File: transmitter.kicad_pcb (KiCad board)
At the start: 6 copper layers, 200 x 110 mm, 244 parts, among them IC1 W9864G6KH-6, IC2 TPS61165DBVR, IC3 MT25QL128ABA1ESE-0SIT, IC4 USBLC6-2SC6, J1 AFC01-S40FCA-00, J2 AFC07-S10ECC-00, J3 B2B-PH-K-S, J4 B2B-PH-K-S, J5 B3B-PH-K-S, J6 USB4085-GF-A, J7 Conn_01x05, J9 Conn_02x06_Odd_Even, Q1 AO3400A, Q2 AO3400A, Q3 SI2301CDS-T1-GE3, Q4 AO3400A, SW1 Button SPST SMD Tactile Switch, SW2 Button SPST SMD Tactile Switch, SW3 Button SPST SMD Tactile Switch, SW4 Button SPST SMD Tactile Switch, SW5 Button SPST SMD Tactile Switch, SW6 Button SPST SMD Tactile Switch, SW7 SW_SPDT_MSM, SW8 Button SPST SMD Tactile Switch, SW9 RotaryEncoder_Switch, U1 STM32H743ZIT6TR, U2 CAT24C256, U3 MP2667GG-0000-Z, U4 AMS1117-3.3, U5 TPS61252DSG, U6 PCA9554APW, Y1 32.768KHZ, Y2 X322525MOB4SI-25MHz

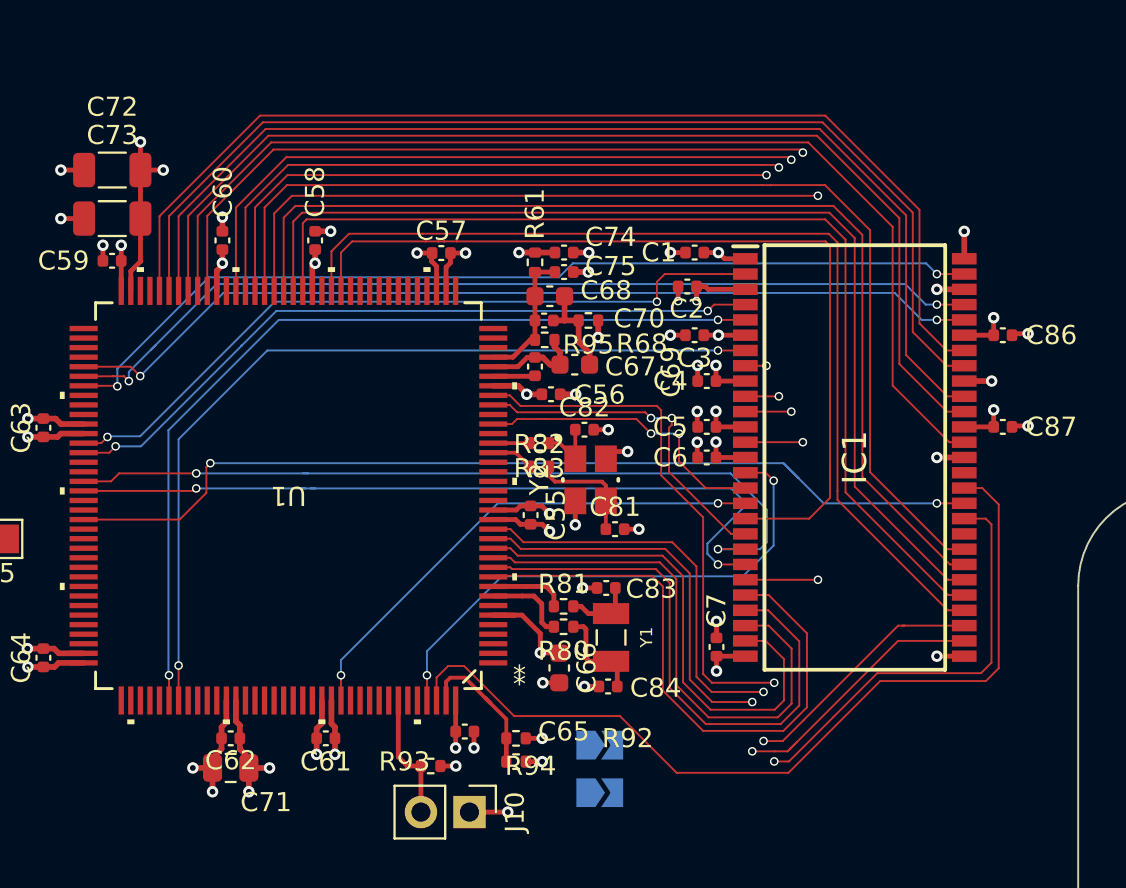
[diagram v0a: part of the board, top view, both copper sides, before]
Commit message: trace length matching sdram, almost done 80%
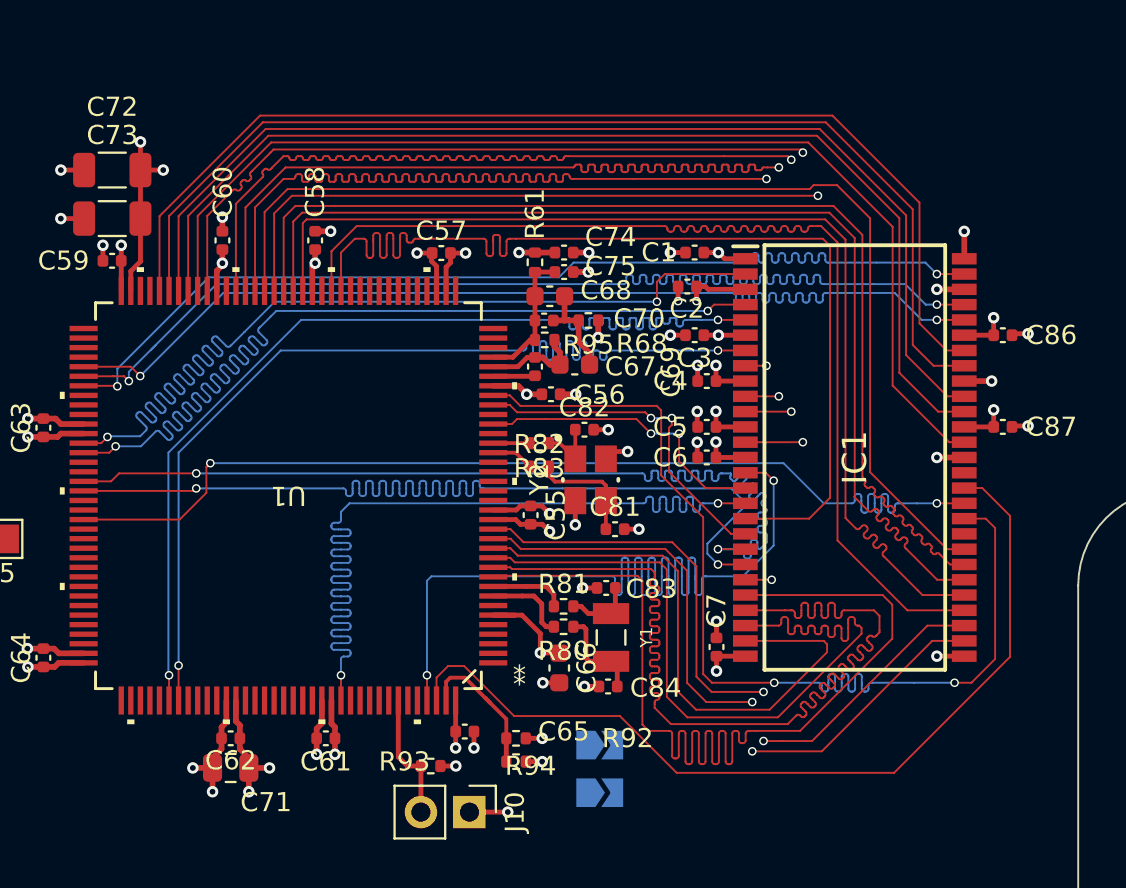
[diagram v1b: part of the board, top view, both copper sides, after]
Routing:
- net /Project Architecture/MCU - IO/FMC_SDNCAS: track 26.7 -> 53.7 mm
- net /Project Architecture/MCU - IO/FMC_A1: track 29.9 -> 56.5 mm
- net /Project Architecture/MCU - IO/FMC_NBL0: track 28.1 -> 53.8 mm
- net /Project Architecture/MCU - IO/FMC_A0: track 31.4 -> 56.9 mm
- net /Project Architecture/MCU - IO/FMC_D1: track 37.9 -> 53.7 mm
- net /Project Architecture/MCU - IO/FMC_D0: track 38.9 -> 53.8 mm
- net /Project Architecture/MCU - IO/FMC_BA1: track 41.1 -> 53.8 mm
- net /Project Architecture/MCU - IO/FMC_A2: track 28.4 -> 40.6 mm
- net /Project Architecture/MCU - IO/FMC_D4: track 42.9 -> 55.0 mm
- net /Project Architecture/MCU - IO/FMC_BA0: track 42.8 -> 53.7 mm
- net /Project Architecture/MCU - IO/FMC_SDNRAS: track 46.0 -> 56.9 mm
- net /Project Architecture/MCU - IO/FMC_D14: track 49.4 -> 60.1 mm
- net /Project Architecture/MCU - IO/FMC_D3: track 45.3 -> 53.8 mm
- net /Project Architecture/MCU - IO/FMC_D5: track 47.0 -> 55.1 mm
- net /Project Architecture/MCU - IO/FMC_D2: track 46.7 -> 53.9 mm
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
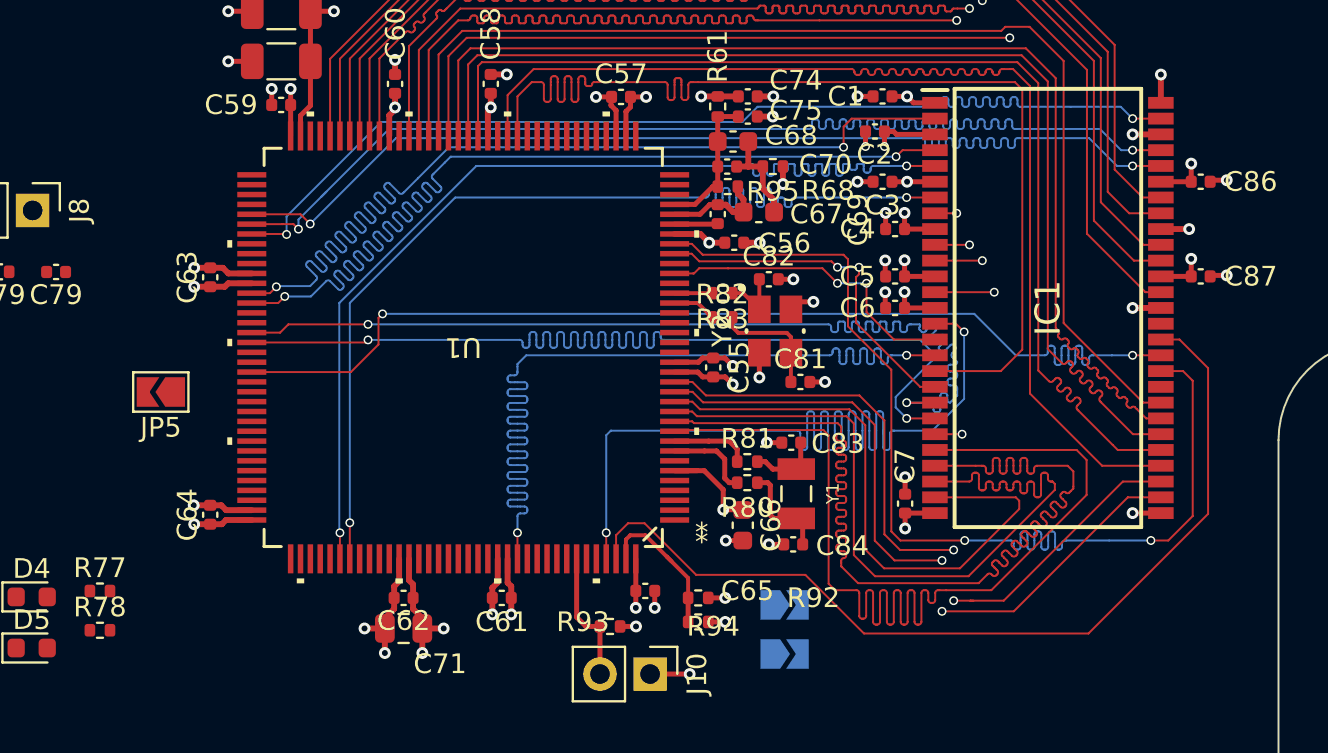
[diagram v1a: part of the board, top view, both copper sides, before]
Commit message: sdram routed and length matching done
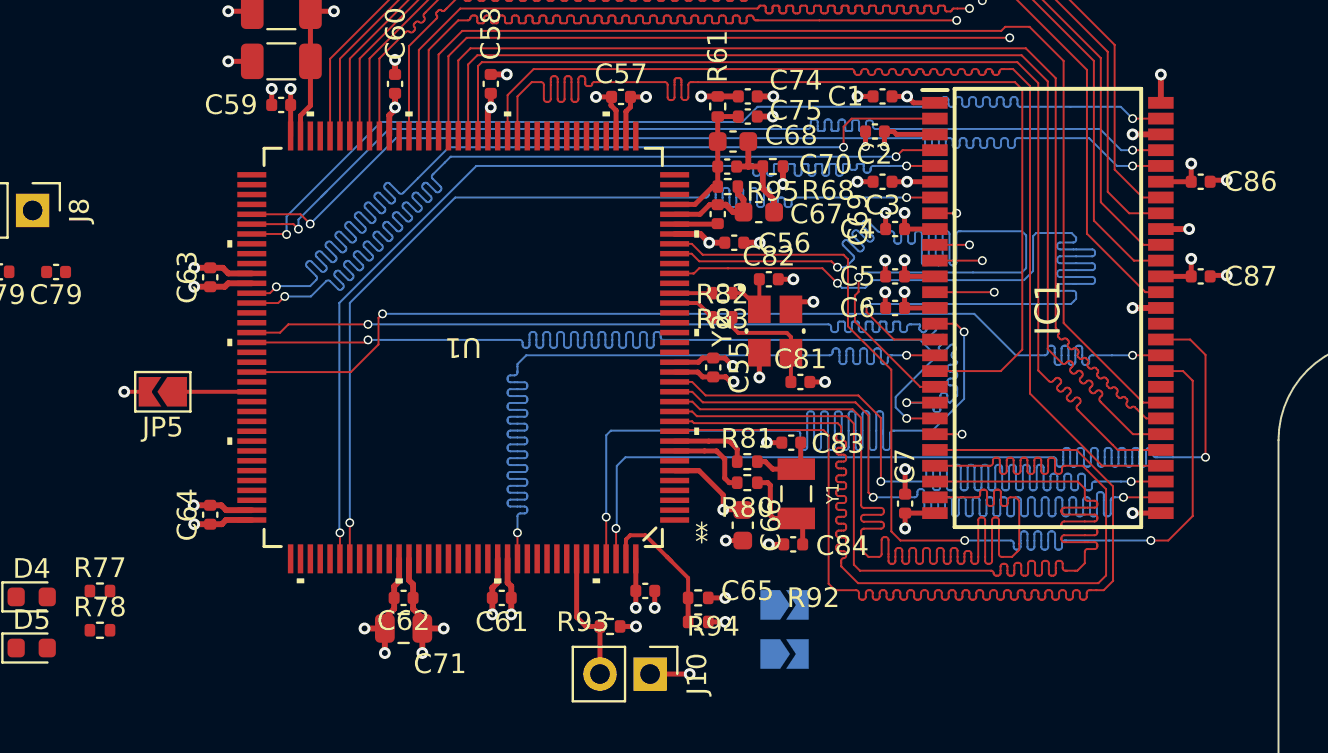
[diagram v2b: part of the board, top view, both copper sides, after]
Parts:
- moved JP5 0.10 mm to (119.9, 84.1)
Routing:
- net /Project Architecture/MCU - IO/FMC_SDNWE: track 15.7 -> 53.9 mm
- net /Project Architecture/MCU - IO/FMC_SDNE0: track 17.9 -> 53.8 mm
- net /Project Architecture/MCU - IO/FMC_A3: track 30.7 -> 56.7 mm
- net /Project Architecture/MCU - IO/FMC_A4: track 36.6 -> 53.7 mm
- net /Project Architecture/MCU - IO/FMC_A5: track 36.8 -> 53.7 mm
- net /Project Architecture/MCU - IO/FMC_A2: track 40.6 -> 56.8 mm
- net /Project Architecture/MCU - IO/FMC_NBL1: track 46.7 -> 53.8 mm, vias 0 -> 2
- net /Project Architecture/MCU - IO/FMC_D14: track 60.1 -> 53.9 mm
- net Net-(JP5-A): track 0.00 -> 3.79 mm
- net +3.3V: track 60.1 -> 61.3 mm, vias 24 -> 25

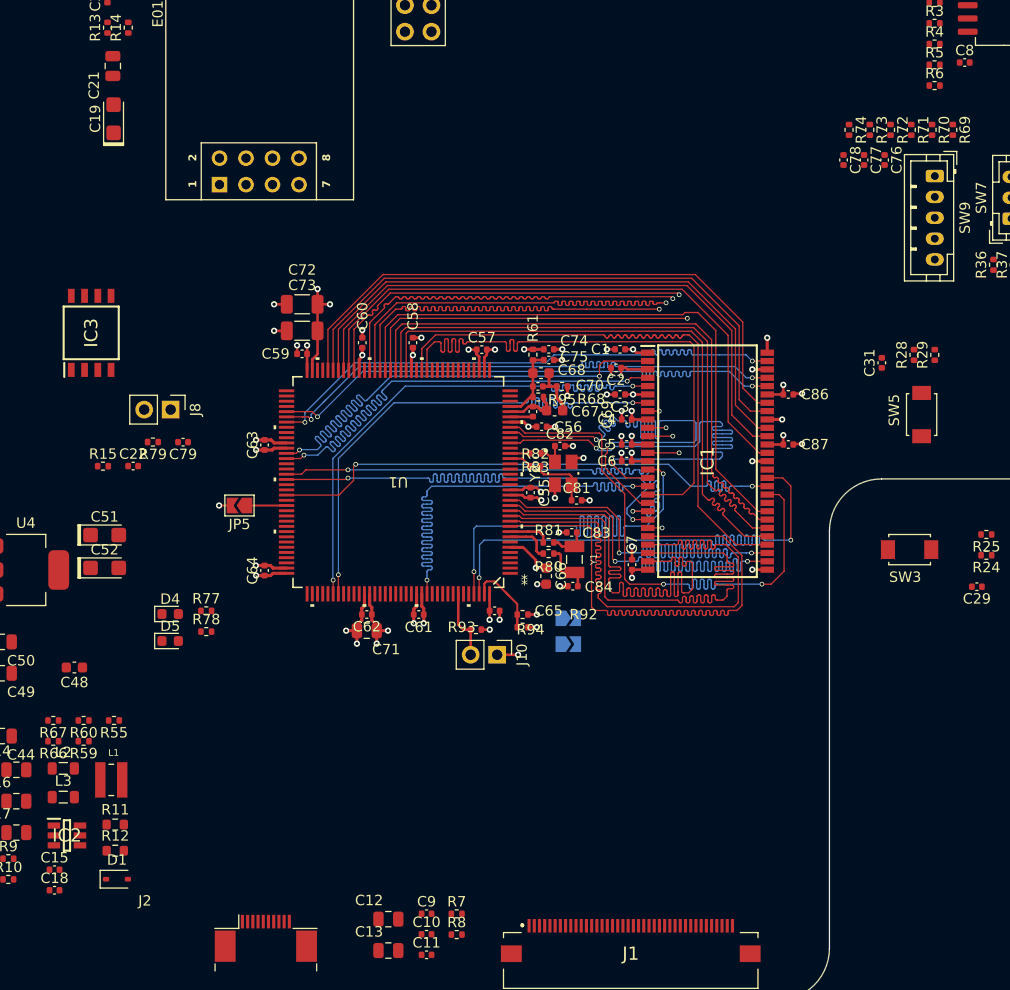
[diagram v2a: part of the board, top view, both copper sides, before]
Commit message: starting layout of lcd connector
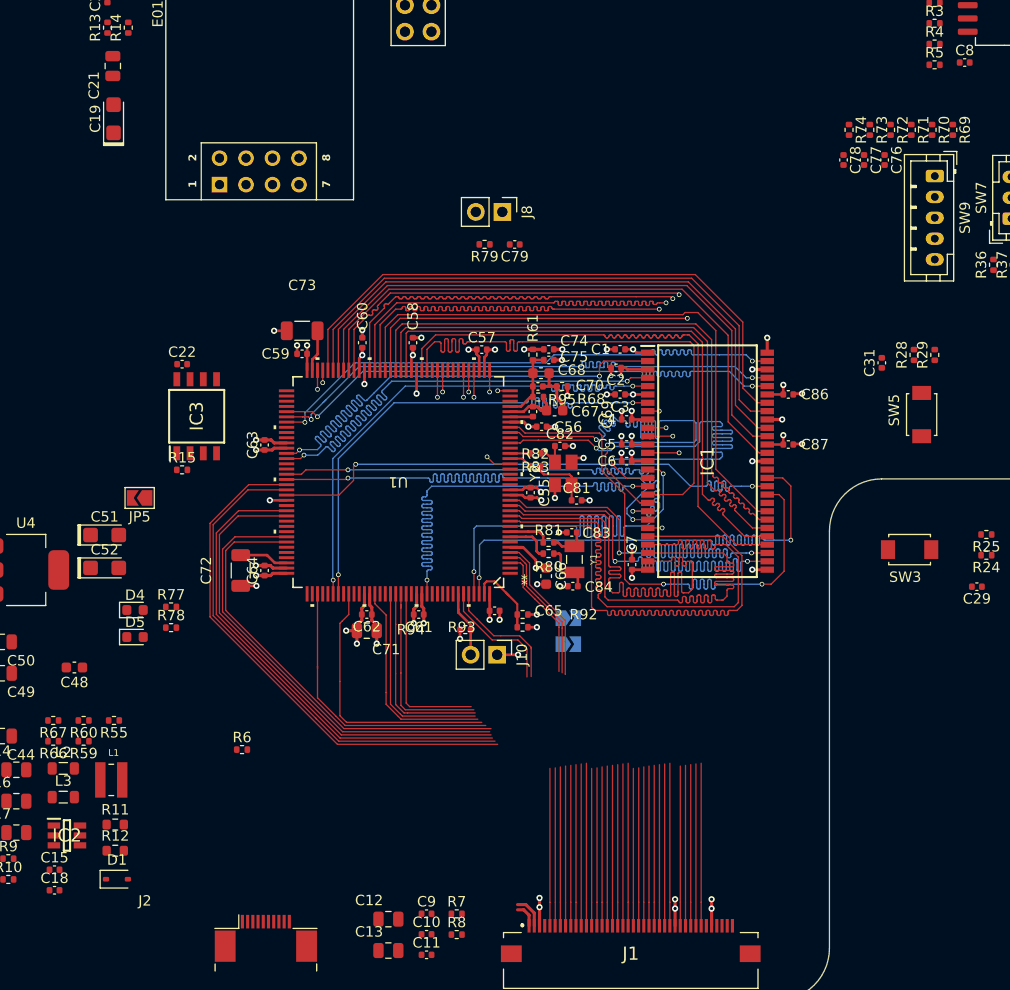
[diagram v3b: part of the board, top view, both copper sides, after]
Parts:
- moved R6 92.0 mm to (120.2, 107.5)
- moved R79 37.0 mm to (143.4, 59.0)
- moved C79 37.0 mm to (146.3, 59.0)
- moved J8 37.0 mm to (145.1, 55.9)
- moved C72 26.2 mm to (120.0, 90.3), turned to -90 degrees
- moved IC3 12.9 mm to (115.8, 75.5)
- moved C22 10.8 mm to (114.4, 70.5)
- moved JP5 9.60 mm to (110.4, 83.3)
- moved R15 7.59 mm to (114.4, 80.6)
- moved R77 3.39 mm to (113.4, 93.8)
- moved R78 3.39 mm to (113.4, 95.8)
- moved D4 3.39 mm to (109.9, 94.1)
- moved D5 3.39 mm to (109.9, 96.7)
- moved R94 1.02 mm to (141.6, 95.9), turned to 180 degrees
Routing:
- net /Project Architecture/LCD - Connectors/LTDC_R7: track 0.00 -> 66.1 mm
- net /Project Architecture/LCD - Connectors/LTDC_CLK: track 0.00 -> 64.6 mm
- net /Project Architecture/LCD - Connectors/LTDC_HSYNC: track 0.00 -> 62.3 mm
- net /Project Architecture/LCD - Connectors/LTDC_G6: track 0.00 -> 61.1 mm
- net /Project Architecture/LCD - Connectors/LTDC_R5: track 0.00 -> 58.5 mm
- net /Project Architecture/LCD - Connectors/LTDC_B1: track 0.00 -> 57.2 mm
- net /Project Architecture/LCD - Connectors/LTDC_VSYNC: track 0.00 -> 51.0 mm, vias 0 -> 1
- net /Project Architecture/LCD - Connectors/LTDC_R6: track 0.00 -> 51.0 mm, vias 0 -> 1
- net /Project Architecture/LCD - Connectors/LTDC_G2: track 0.00 -> 50.5 mm, vias 0 -> 1
- net /Project Architecture/LCD - Connectors/LTDC_R4: track 0.00 -> 50.4 mm, vias 0 -> 1
- net /Project Architecture/LCD - Connectors/LTDC_R3: track 0.00 -> 50.3 mm, vias 0 -> 1
- net /Project Architecture/LCD - Connectors/LTDC_B5: track 0.00 -> 49.9 mm, vias 0 -> 1
- net /Project Architecture/LCD - Connectors/LTDC_R1: track 0.00 -> 48.2 mm, vias 0 -> 1
- net /Project Architecture/LCD - Connectors/LTDC_G5: track 0.00 -> 47.5 mm, vias 0 -> 1
- net /Project Architecture/LCD - Connectors/LTDC_G4: track 0.00 -> 47.2 mm, vias 0 -> 1
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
